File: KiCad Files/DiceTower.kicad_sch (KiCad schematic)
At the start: 3 parts, among them U1 NHD-0420H1Z

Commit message: Add system diagram
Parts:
- added J1: Conn_02x07_Counter_Clockwise, Connector_PinHeader_2.54mm:PinHeader_2x07_P2.54mm_Vertical, symbol Connector_Generic:Conn_02x07_Counter_Clockwise
- added U2: ESP32-DevKitC, Espressif:ESP32-DevKitC, symbol PCM_Espressif:ESP32-DevKitC
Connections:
- net DB0: now also U2.10 (DAC_2/ADC2_CH9/GPIO26); no longer A1.25 (A12/IO13)
- net DB1: now also U2.9 (DAC_1/ADC2_CH8/GPIO25); no longer A1.24 (A11/IO12)
- net DB2: now also U2.11 (ADC2_CH7/GPIO27); no longer A1.18 (SCL/IO22)
- net DB3: now also U2.30 (GPIO18); no longer A1.19 (A6/IO14)
- net DB4: now also U2.31 (GPIO19); no longer A1.20 (A7/IO32)
- net DB5: now also U2.33 (GPIO21); no longer A1.21 (A8/IO15)
- net DB6: now also U2.36 (GPIO22); no longer A1.22 (A9/IO33)
- net DB7: now also U2.37 (GPIO23); no longer A1.23 (A10/IO27)
- net at U1.4 (RS): now also U2.26 (ADC2_CH0/GPIO4); no longer A1.11 (SCK/IO5)
- net at U1.5 (R/W): now also U2.27 (GPIO16); no longer A1.12 (MOSI/IO18)
- net at U1.6 (E): now also U2.28 (GPIO17); no longer A1.13 (MISO/IO19)
- new net: U2.14 (GND), U2.32 (GND), U2.38 (GND)
- no-connect marks 0 -> 11
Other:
- moved on the sheet: A1

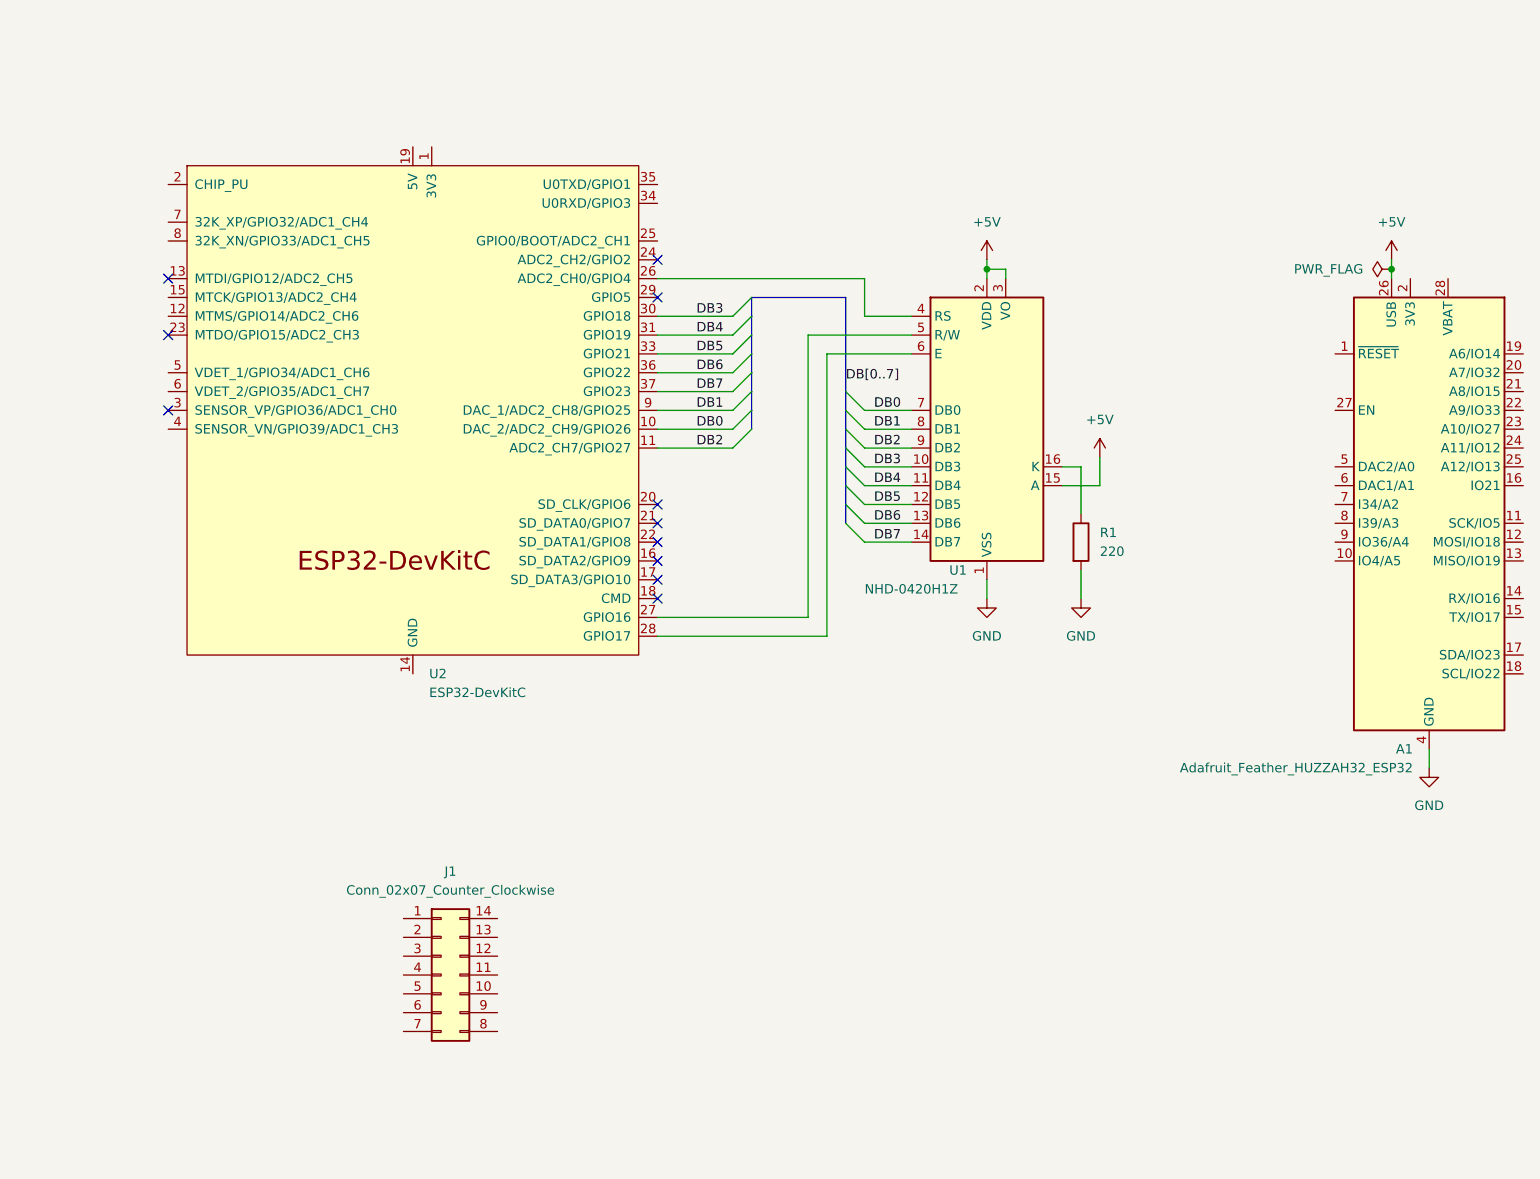
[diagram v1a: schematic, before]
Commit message: Add BOM, updated schematics
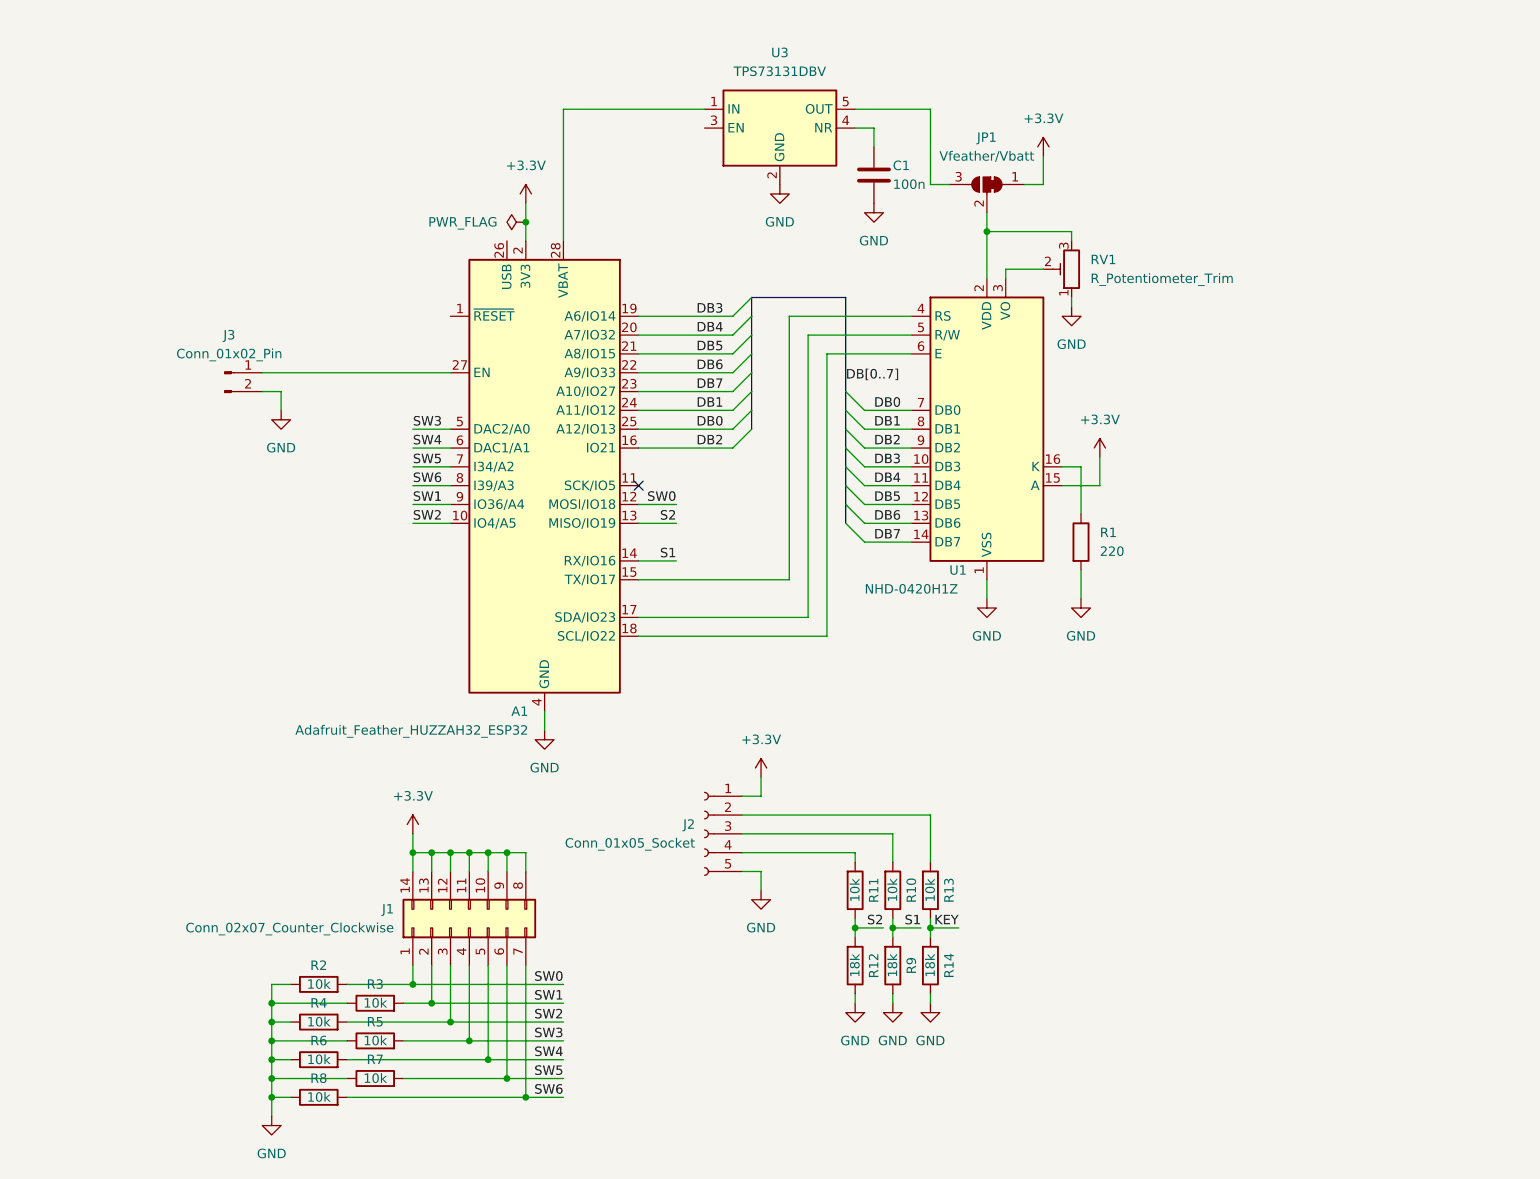
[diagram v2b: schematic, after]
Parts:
- removed U2: ESP32-DevKitC, Espressif:ESP32-DevKitC, symbol PCM_Espressif:ESP32-DevKitC
- added C1: 100n, symbol Device:C
- added J2: Conn_01x05_Socket, Connector_PinSocket_2.54mm:PinSocket_1x05_P2.54mm_Vertical, symbol Connector:Conn_01x05_Socket
- added J3: Conn_01x02_Pin, Connector_PinHeader_2.54mm:PinHeader_1x02_P2.54mm_Vertical, symbol Connector:Conn_01x02_Pin
- added JP1: Vfeather/Vbatt, symbol Jumper:SolderJumper_3_Bridged12
- added R10, R11, R13, R2, R3, R4, R5, R6, R7, R8: 10k, symbol Device:R
- added R12, R14, R9: 18k, symbol Device:R
- added RV1: R_Potentiometer_Trim, symbol Device:R_Potentiometer_Trim
- added U3: TPS73131DBV, Package_TO_SOT_SMD:SOT-23-5, symbol Regulator_Linear:TPS73131DBV
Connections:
- net DB0: now also A1.25 (A12/IO13)
- net DB1: now also A1.24 (A11/IO12)
- net DB2: now also A1.16 (IO21)
- net DB3: now also A1.19 (A6/IO14)
- net DB4: now also A1.20 (A7/IO32)
- net DB5: now also A1.21 (A8/IO15)
- net DB6: now also A1.22 (A9/IO33)
- net DB7: now also A1.23 (A10/IO27)
- net GND: now also C1.2, J2.5 (Pin_5), J3.2 (Pin_2), R12.1, R14.1, R2.1, R3.1, R4.1, R5.1, R6.1, R7.1, R8.1, R9.1, RV1.1, U3.2 (GND)
- net at U1.4 (RS): now also A1.15 (TX/IO17)
- net at U1.5 (R/W): now also A1.17 (SDA/IO23)
- net at U1.6 (E): now also A1.18 (SCL/IO22)
- net SW0: now reaches J1.1 (Pin_1)
- net SW0: now also A1.12 (MOSI/IO18), R2.2
- net +3.3V: now reaches J1.10 (Pin_10)
- net +3.3V: now also A1.2 (3V3), J1.11 (Pin_11), J1.12 (Pin_12), J1.13 (Pin_13), J1.14 (Pin_14), J1.8 (Pin_8), J1.9 (Pin_9), U1.15 (A), J2.1 (Pin_1), JP1.1 (A)
- net SW1: now reaches J1.2 (Pin_2)
- net SW1: now also A1.9 (IO36/A4), R3.2
- net SW2: now reaches J1.3 (Pin_3)
- net SW2: now also A1.10 (IO4/A5), R4.2
- net SW3: now reaches J1.4 (Pin_4)
- net SW3: now also A1.5 (DAC2/A0), R5.2
- net SW4: now reaches J1.5 (Pin_5)
- net SW4: now also A1.6 (DAC1/A1), R6.2
- net SW5: now reaches J1.6 (Pin_6)
- net SW5: now also A1.7 (I34/A2), R7.2
- net SW6: now reaches J1.7 (Pin_7)
- net SW6: now also A1.8 (I39/A3), R8.2
- net S2: now reaches A1.13 (MISO/IO19)
- net S2: now also R11.1, R12.2
- net S1: now reaches A1.14 (RX/IO16)
- net S1: now also R10.1, R9.2
- net at A1.27 (EN): now also J3.1 (Pin_1)
- net at A1.28 (VBAT): now also U3.1 (IN)
- removed net +5V: A1.26 (USB), U1.15 (A), U1.2 (VDD), U1.3 (VO)
- new net: J2.4 (Pin_4), R11.2
- new net: J2.2 (Pin_2), R13.2
- new net: J2.3 (Pin_3), R10.2
- new net: C1.1, U3.4 (NR)
- new net: JP1.2 (C), RV1.3, U1.2 (VDD)
- new net: RV1.2, U1.3 (VO)
- new net: JP1.3 (B), U3.5 (OUT)
- new net KEY: R13.1, R14.2
- no-connect marks 11 -> 1
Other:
- moved on the sheet: J1

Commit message: Update BOM
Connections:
- net at A1.28 (VBAT), U3.1 (IN): now also U3.3 (EN)
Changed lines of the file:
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@@
   (junction (at 129.54 135.89) (diameter 0) (color 0 0 0 0)
+  )
+  (junction (at 101.6 25.4) (diameter 0) (color 0 0 0 0)
   )
   (junction (at 124.46 135.89) (diameter 0) (color 0 0 0 0)
@@
     (stroke (width 0) (type default))
   )
-  (wire (pts (xy 85.09 25.4) (xy 104.14 25.4))
+  (wire (pts (xy 85.09 25.4) (xy 101.6 25.4))
     (stroke (width 0) (type default))
   )
@@
     (stroke (width 0) (type default))
   )
+  (wire (pts (xy 101.6 25.4) (xy 104.14 25.4))
+    (stroke (width 0) (type default))
+  )
   (wire (pts (xy 85.09 25.4) (xy 85.09 43.18))
     (stroke (width 0) (type default))
@@
     (stroke (width 0) (type default))
   )
+  (wire (pts (xy 101.6 27.94) (xy 101.6 25.4))
+    (stroke (width 0) (type default))
+  )
   (wire (pts (xy 64.77 76.2) (xy 69.85 76.2))
     (stroke (width 0) (type default))
@@
     (stroke (width 0) (type default))
   )
+  (wire (pts (xy 104.14 27.94) (xy 101.6 27.94))
+    (stroke (width 0) (type default))
+  )

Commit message: Add PCB
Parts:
- removed J1: Conn_02x07_Counter_Clockwise, Connector_PinHeader_2.54mm:PinHeader_2x07_P2.54mm_Vertical, symbol Connector_Generic:Conn_02x07_Counter_Clockwise
- added J1: Conn_02x07_Odd_Even, Connector_PinHeader_2.54mm:PinHeader_2x07_P2.54mm_Vertical, symbol Connector_Generic:Conn_02x07_Odd_Even
- added JP2: SolderJumper_2_Open, Jumper:SolderJumper-2_P1.3mm_Open_RoundedPad1.0x1.5mm, symbol Jumper:SolderJumper_2_Open
- C1: footprint (none) -> Capacitor_SMD:C_0603_1608Metric
- JP1: footprint (none) -> Jumper:SolderJumper-3_P1.3mm_Bridged12_RoundedPad1.0x1.5mm_NumberLabels
- R1, R10, R11, R12, R13, R14, R2, R3, R4, R5, R6, R7, R8, R9: footprint (none) -> PCM_Resistor_SMD_AKL:R_0603_1608Metric
- RV1: footprint (none) -> PCM_Potentiometer_THT_AKL:Potentiometer_Bourns_3266W_Vertical
- U1: footprint Display:NHD-0420H1Z -> Connector_PinHeader_2.54mm:PinHeader_1x16_P2.54mm_Vertical
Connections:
- net +3.3V: now also J1.1 (Pin_1), J1.11 (Pin_11), J1.13 (Pin_13), J1.3 (Pin_3), J1.5 (Pin_5), J1.7 (Pin_7), J1.9 (Pin_9)
- net DB5: now also A1.19 (A6/IO14); no longer A1.21 (A8/IO15)
- net GND: now also JP2.1 (A)
- net SW0: now also J1.2 (Pin_2)
- net SW1: now also J1.4 (Pin_4)
- net SW2: now also J1.6 (Pin_6)
- net SW3: now also J1.8 (Pin_8)
- net SW4: now also J1.10 (Pin_10)
- net SW5: now also J1.12 (Pin_12)
- net SW6: now also J1.14 (Pin_14)
- net at R1.1, U1.16 (K): now also JP2.2 (B)
- net DB0: no longer names the net of A1.25 (A12/IO13)
- net DB0: no longer U1.7 (DB0)
- net DB1: no longer names the net of A1.24 (A11/IO12)
- net DB1: no longer U1.8 (DB1)
- net DB2: no longer names the net of A1.16 (IO21)
- net DB2: no longer U1.9 (DB2)
- net DB3: no longer names the net of U1.10 (DB3)
- net DB3: no longer A1.19 (A6/IO14)
- no-connect marks 1 -> 8

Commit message: Cleanup
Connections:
- net KEY: now also A1.16 (IO21)
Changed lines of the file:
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@@
+    (stroke (width 0) (type default))
+  )
+  (wire (pts (xy 95.25 71.12) (xy 100.33 71.12))
     (stroke (width 0) (type default))
   )
@@
     (effects (font (size 1.27 1.27)) (justify right bottom))
   )
+  (label "KEY" (at 100.33 71.12 180) (fields_autoplaced)
+    (effects (font (size 1.27 1.27)) (justify right bottom))
+  )

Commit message: Octagon
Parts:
- removed J1: Conn_02x07_Odd_Even, Connector_PinHeader_2.54mm:PinHeader_2x07_P2.54mm_Vertical, symbol Connector_Generic:Conn_02x07_Odd_Even
- removed R10, R11, R13: 10k, PCM_Resistor_SMD_AKL:R_0603_1608Metric, symbol Device:R
- removed R12, R14, R9: 18k, PCM_Resistor_SMD_AKL:R_0603_1608Metric, symbol Device:R
- added SW0, SW1, SW2, SW3, SW4, SW5, SW6: ChMxBl, Button_Switch_Keyboard:SW_Cherry_MX_1.00u_PCB, symbol Switch:SW_Push
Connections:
- net +3.3V: now also SW0.2, SW1.2, SW2.2, SW3.2, SW4.2, SW5.2, SW6.2
- net DB4: now also A1.19 (A6/IO14); no longer A1.20 (A7/IO32)
- net DB5: now also A1.20 (A7/IO32); no longer A1.19 (A6/IO14)
- net KEY: now also J2.2 (Pin_2)
- net S1: now also J2.3 (Pin_3)
- net S2: now also J2.4 (Pin_4)
- net SW0: now also A1.5 (DAC2/A0), SW0.1; no longer A1.12 (MOSI/IO18)
- net SW1: now also A1.6 (DAC1/A1), SW1.1; no longer A1.9 (IO36/A4)
- net SW2: now also A1.7 (I34/A2), SW2.1; no longer A1.10 (IO4/A5)
- net SW3: now also A1.8 (I39/A3), SW3.1; no longer A1.5 (DAC2/A0)
- net SW4: now also A1.9 (IO36/A4), SW4.1; no longer A1.6 (DAC1/A1)
- net SW5: now also A1.10 (IO4/A5), SW5.1; no longer A1.7 (I34/A2)
- net SW6: now also A1.12 (MOSI/IO18), SW6.1; no longer A1.8 (I39/A3)
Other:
- moved on the sheet: J2, R2, R3, R4, R5, R6, R7, R8

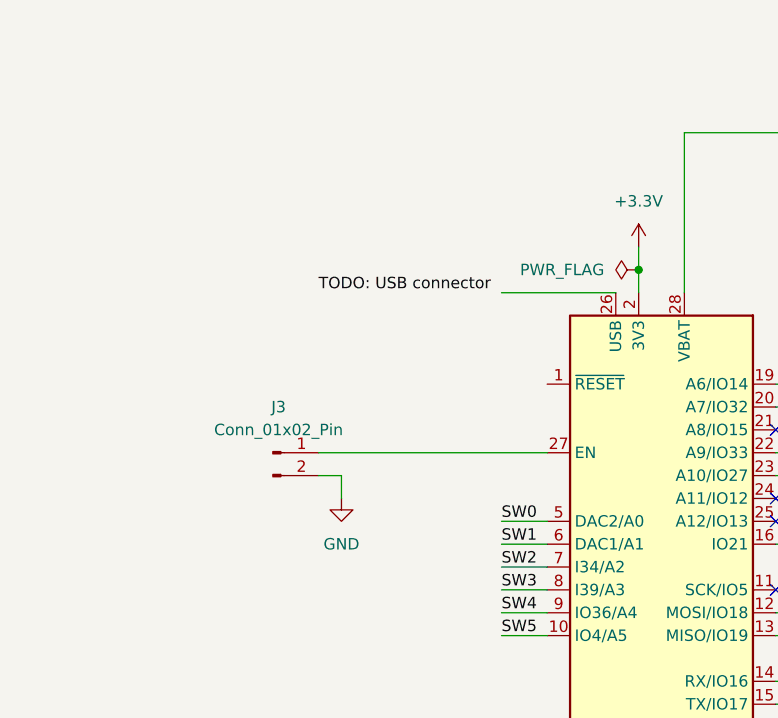
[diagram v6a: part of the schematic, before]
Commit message: Added usb-c connector
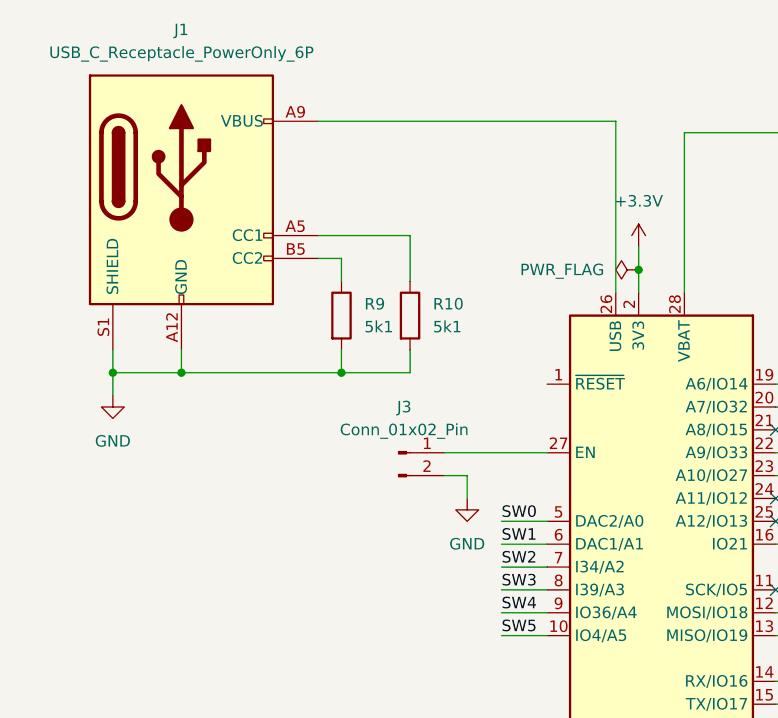
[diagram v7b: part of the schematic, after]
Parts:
- added J1: USB_C_Receptacle_PowerOnly_6P, Connector_USB:USB_C_Receptacle_GCT_USB4125-xx-x-0190_6P_TopMnt_Horizontal, symbol Connector:USB_C_Receptacle_PowerOnly_6P
- added R10, R9: 5k1, Resistor_SMD:R_0603_1608Metric_Pad0.98x0.95mm_HandSolder, symbol Device:R
- R1, R2, R3, R4, R5, R6, R7, R8: footprint PCM_Resistor_SMD_AKL:R_0603_1608Metric -> Resistor_SMD:R_0603_1608Metric_Pad0.98x0.95mm_HandSolder
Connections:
- net GND: now also J1.A12 (GND), J1.B12 (GND), J1.S1 (SHIELD), R10.2, R9.2
- net at A1.26 (USB): now also J1.A9 (VBUS), J1.B9 (VBUS)
- new net: J1.B5 (CC2), R9.1
- new net: J1.A5 (CC1), R10.1
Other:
- moved on the sheet: J3
